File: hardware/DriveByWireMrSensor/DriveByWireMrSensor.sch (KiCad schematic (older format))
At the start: 7 parts, among them J1 Conn_01x04_Female, U1 LM358, U2 KMZ49_118

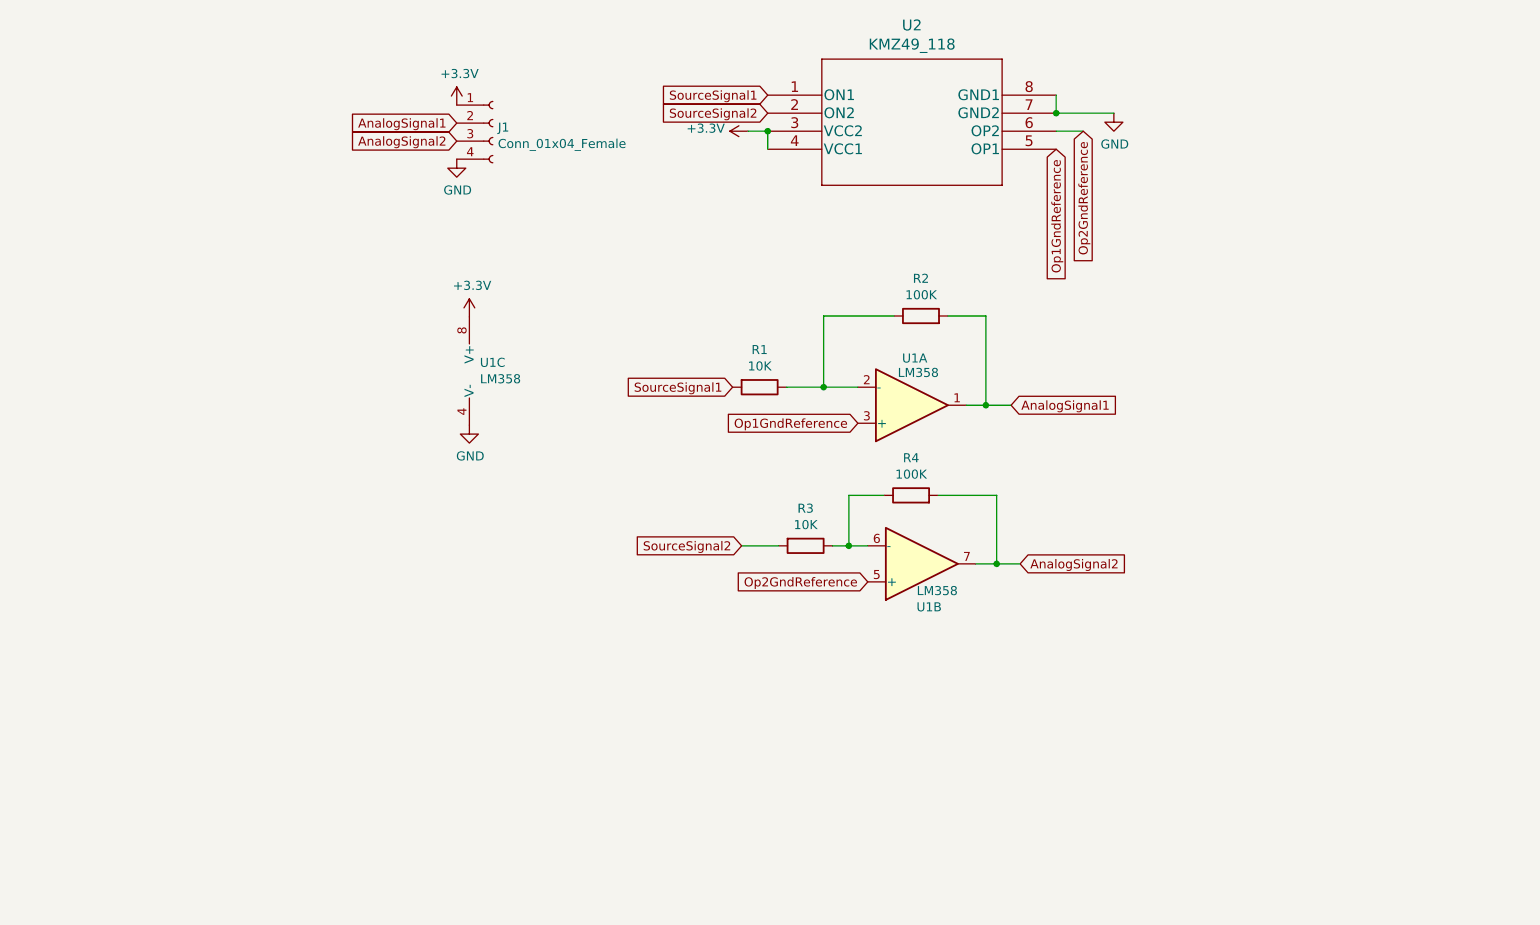
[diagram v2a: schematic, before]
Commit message: fixing drive by wire PCB to make space for shim and avoiding screw holes
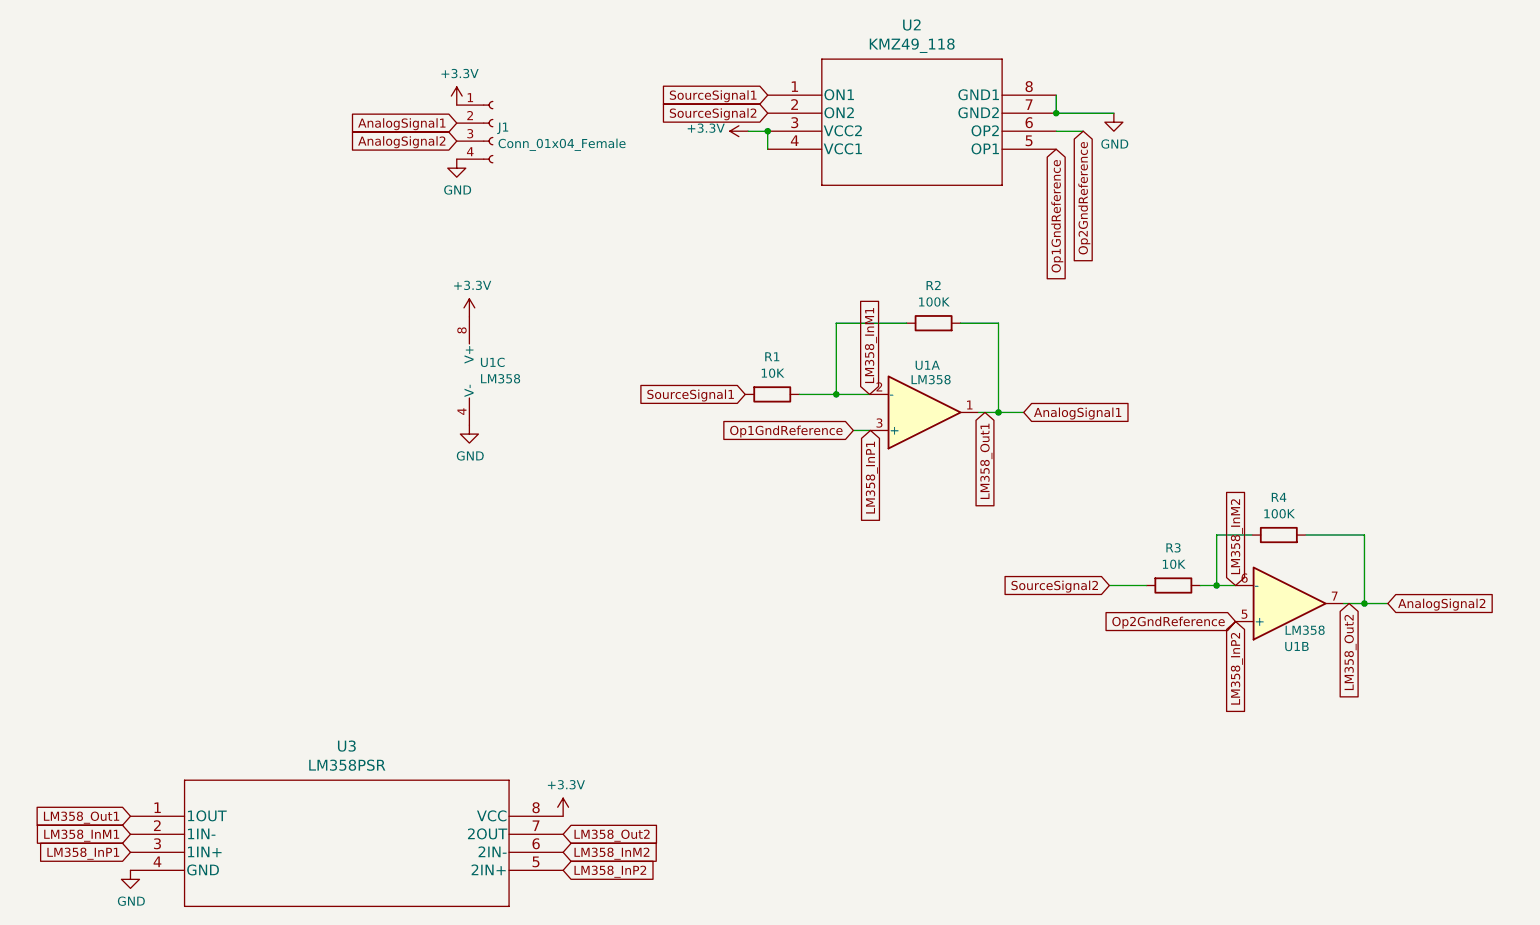
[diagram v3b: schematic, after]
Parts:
- added U3: LM358PSR, UsefulModifications:DFN-8-LM358, symbol LM358:LM358PSR
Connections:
- net +3V3: now also U3.8 (VCC)
- net AnalogSignal1: now also U3.1 (1OUT)
- net AnalogSignal2: now also U3.7 (2OUT)
- net GND: now also U3.4 (GND)
- net LM358_InM1: now reaches R1.1, R2.1, U1.2 (-)
- net LM358_InM1: now also U3.2 (1IN-)
- net LM358_InM2: now reaches R3.1, R4.1, U1.6 (-)
- net LM358_InM2: now also U3.6 (2IN-)
- net Op1GndReference renamed LM358_InP1
- net LM358_InP1: now also U3.3 (1IN+)
- net Op2GndReference renamed LM358_InP2
- net LM358_InP2: now also U3.5 (2IN+)
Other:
- moved on the sheet: R1, R2, R3, R4, U1A, U1B
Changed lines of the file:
@@
 L Device:R R1
 U 1 1 6189DE68
-P 5150 4080
-F 0 "R1" V 4943 4080 50  0000 C CNN
-F 1 "10K" V 5034 4080 50  0000 C CNN
-F 2 "Resistor_SMD:R_0805_2012Metric_Pad1.15x1.40mm_HandSolder" V 5080 4080 50  0001 C CNN
-F 3 "~" H 5150 4080 50  0001 C CNN
-	1    5150 4080
+P 5220 4120
+F 0 "R1" V 5013 4120 50  0000 C CNN
+F 1 "10K" V 5104 4120 50  0000 C CNN
+F 2 "Resistor_SMD:R_0805_2012Metric_Pad1.15x1.40mm_HandSolder" V 5150 4120 50  0001 C CNN
+F 3 "~" H 5220 4120 50  0001 C CNN
+	1    5220 4120
 	0    1    1    0
 $EndComp
@@
 L Device:R R2
 U 1 1 6189E497
-P 6045 3685
-F 0 "R2" V 6252 3685 50  0000 C CNN
-F 1 "100K" V 6161 3685 50  0000 C CNN
-F 2 "Resistor_SMD:R_0805_2012Metric_Pad1.15x1.40mm_HandSolder" V 5975 3685 50  0001 C CNN
-F 3 "~" H 6045 3685 50  0001 C CNN
-	1    6045 3685
+P 6115 3725
+F 0 "R2" V 6322 3725 50  0000 C CNN
+F 1 "100K" V 6231 3725 50  0000 C CNN
+F 2 "Resistor_SMD:R_0805_2012Metric_Pad1.15x1.40mm_HandSolder" V 6045 3725 50  0001 C CNN
+F 3 "~" H 6115 3725 50  0001 C CNN
+	1    6115 3725
 	0    -1   -1   0
 $EndComp
@@
 	1    0    0    -1
 $EndComp
-Text GLabel 6545 4180 2    50   Input ~ 0
+Text GLabel 6615 4220 2    50   Input ~ 0
 AnalogSignal1
 Text GLabel 6795 2760 3    50   Input ~ 0
 Op1GndReference
-Text GLabel 5695 4280 0    50   Input ~ 0
+Text GLabel 5670 4320 0    50   Input ~ 0
 Op1GndReference
 Text GLabel 5195 2460 0    50   Input ~ 0
 SourceSignal1
-Text GLabel 5000 4080 0    50   Input ~ 0
+Text GLabel 5070 4120 0    50   Input ~ 0
 SourceSignal1
 $Comp
 L Amplifier_Operational:LM358 U1
 U 1 1 618B4249
-P 5995 4180
-F 0 "U1" H 6010 3920 50  0000 C CNN
-F 1 "LM358" H 6030 4000 50  0000 C CNN
-F 2 "UsefulModifications:LM358PSR" H 5995 4180 50  0001 C CNN
-F 3 "http://www.ti.com/lit/ds/symlink/lm2904-n.pdf" H 5995 4180 50  0001 C CNN
-	1    5995 4180
+P 6065 4220
+F 0 "U1" H 6080 3960 50  0000 C CNN
+F 1 "LM358" H 6100 4040 50  0000 C CNN
+F 2 "UsefulModifications:LM358PSR" H 6065 4220 50  0001 C CNN
+F 3 "http://www.ti.com/lit/ds/symlink/lm2904-n.pdf" H 6065 4220 50  0001 C CNN
+	1    6065 4220
 	1    0    0    1
 $EndComp
@@
 $EndComp
 Wire Wire Line
-	6295 4180 6405 4180
-Wire Wire Line
-	6195 3685 6405 3685
-Wire Wire Line
-	6405 3685 6405 4180
-Connection ~ 6405 4180
-Wire Wire Line
-	6405 4180 6545 4180
-Wire Wire Line
-	5505 4080 5695 4080
-Wire Wire Line
-	5505 3685 5505 4080
-Wire Wire Line
-	5895 3685 5505 3685
-Wire Wire Line
-	5300 4080 5505 4080
-Connection ~ 5505 4080
+	6365 4220 6475 4220
+Wire Wire Line
+	6265 3725 6475 3725
+Wire Wire Line
+	6475 3725 6475 4220
+Connection ~ 6475 4220
+Wire Wire Line
+	6475 4220 6615 4220
+Wire Wire Line
+	5575 4120 5765 4120
+Wire Wire Line
+	5575 3725 5575 4120
+Wire Wire Line
+	5965 3725 5575 3725
+Wire Wire Line
+	5370 4120 5575 4120
+Connection ~ 5575 4120
 $Comp
 L power:+3.3V #PWR0106
@@
 L Amplifier_Operational:LM358 U1
 U 2 1 618E9970
-P 6050 5060
-F 0 "U1" H 6090 5300 50  0000 C CNN
-F 1 "LM358" H 6135 5210 50  0000 C CNN
-F 2 "UsefulModifications:LM358PSR" H 6050 5060 50  0001 C CNN
-F 3 "http://www.ti.com/lit/ds/symlink/lm2904-n.pdf" H 6050 5060 50  0001 C CNN
-	2    6050 5060
+P 8090 5280
+F 0 "U1" H 8130 5520 50  0000 C CNN
+F 1 "LM358" H 8175 5430 50  0000 C CNN
+F 2 "UsefulModifications:LM358PSR" H 8090 5280 50  0001 C CNN
+F 3 "http://www.ti.com/lit/ds/symlink/lm2904-n.pdf" H 8090 5280 50  0001 C CNN
+	2    8090 5280
 	1    0    0    1
 $EndComp
@@
 L Device:R R4
 U 1 1 618DED44
-P 5990 4680
-F 0 "R4" V 6197 4680 50  0000 C CNN
-F 1 "100K" V 6106 4680 50  0000 C CNN
-F 2 "Resistor_SMD:R_0805_2012Metric_Pad1.15x1.40mm_HandSolder" V 5920 4680 50  0001 C CNN
-F 3 "~" H 5990 4680 50  0001 C CNN
-	1    5990 4680
+P 8030 4900
+F 0 "R4" V 8237 4900 50  0000 C CNN
+F 1 "100K" V 8146 4900 50  0000 C CNN
+F 2 "Resistor_SMD:R_0805_2012Metric_Pad1.15x1.40mm_HandSolder" V 7960 4900 50  0001 C CNN
+F 3 "~" H 8030 4900 50  0001 C CNN
+	1    8030 4900
 	0    -1   -1   0
 $EndComp
@@
 L Device:R R3
 U 1 1 618E050D
-P 5405 4960
-F 0 "R3" V 5198 4960 50  0000 C CNN
-F 1 "10K" V 5289 4960 50  0000 C CNN
-F 2 "Resistor_SMD:R_0805_2012Metric_Pad1.15x1.40mm_HandSolder" V 5335 4960 50  0001 C CNN
-F 3 "~" H 5405 4960 50  0001 C CNN
-	1    5405 4960
+P 7445 5180
+F 0 "R3" V 7238 5180 50  0000 C CNN
+F 1 "10K" V 7329 5180 50  0000 C CNN
+F 2 "Resistor_SMD:R_0805_2012Metric_Pad1.15x1.40mm_HandSolder" V 7375 5180 50  0001 C CNN
+F 3 "~" H 7445 5180 50  0001 C CNN
+	1    7445 5180
 	0    1    1    0
 $EndComp
@@
 Text GLabel 5195 2560 0    50   Input ~ 0
 SourceSignal2
-Text GLabel 5050 4960 0    50   Input ~ 0
+Text GLabel 7090 5180 0    50   Input ~ 0
 SourceSignal2
-Text GLabel 5750 5160 0    50   Input ~ 0
+Text GLabel 7790 5380 0    50   Input ~ 0
 Op2GndReference
-Text GLabel 6595 5060 2    50   Input ~ 0
+Text GLabel 8635 5280 2    50   Input ~ 0
 AnalogSignal2
 Wire Wire Line
-	6350 5060 6465 5060
-Wire Wire Line
-	6140 4680 6465 4680
-Wire Wire Line
-	6465 4680 6465 5060
-Connection ~ 6465 5060
-Wire Wire Line
-	6465 5060 6595 5060
-Wire Wire Line
-	5555 4960 5645 4960
-Wire Wire Line
-	5840 4680 5645 4680
-Wire Wire Line
-	5645 4680 5645 4960
-Connection ~ 5645 4960
-Wire Wire Line
-	5645 4960 5750 4960
-Wire Wire Line
-	5050 4960 5255 4960
+	8390 5280 8505 5280
+Wire Wire Line
+	8180 4900 8505 4900
+Wire Wire Line
+	8505 4900 8505 5280
+Connection ~ 8505 5280
+Wire Wire Line
+	8505 5280 8635 5280
+Wire Wire Line
+	7595 5180 7685 5180
+Wire Wire Line
+	7880 4900 7685 4900
+Wire Wire Line
+	7685 4900 7685 5180
+Connection ~ 7685 5180
+Wire Wire Line
+	7685 5180 7790 5180
+Wire Wire Line
+	7090 5180 7295 5180
+$Comp
+L LM358:LM358PSR U3
+U 1 1 619970C4
+P 1660 6460
+F 0 "U3" H 2860 6847 60  0000 C CNN
+F 1 "LM358PSR" H 2860 6741 60  0000 C CNN
+F 2 "UsefulModifications:DFN-8-LM358" H 2860 6700 60  0001 C CNN
+F 3 "" H 1660 6460 60  0000 C CNN
+	1    1660 6460
+	1    0    0    -1
+$EndComp
+$Comp
+L power:GND #PWR0107
+U 1 1 61998A96
+P 1660 6760
+F 0 "#PWR0107" H 1660 6510 50  0001 C CNN
+F 1 "GND" H 1665 6587 50  0000 C CNN
+F 2 "" H 1660 6760 50  0001 C CNN
+F 3 "" H 1660 6760 50  0001 C CNN
+	1    1660 6760
+	1    0    0    -1
+$EndComp
+$Comp
+L power:+3.3V #PWR0108
+U 1 1 61999CB9
+P 4060 6460
+F 0 "#PWR0108" H 4060 6310 50  0001 C CNN
+F 1 "+3.3V" H 4075 6633 50  0000 C CNN
+F 2 "" H 4060 6460 50  0001 C CNN
+F 3 "" H 4060 6460 50  0001 C CNN
+	1    4060 6460
+	1    0    0    -1
+$EndComp
+Text GLabel 4060 6560 2    50   Input ~ 0
+LM358_Out2
+Text GLabel 4060 6660 2    50   Input ~ 0
+LM358_InM2
+Text GLabel 4060 6760 2    50   Input ~ 0
+LM358_InP2
+Text GLabel 1660 6460 0    50   Input ~ 0
+LM358_Out1
+Text GLabel 1660 6560 0    50   Input ~ 0
+LM358_InM1
+Text GLabel 1660 6660 0    50   Input ~ 0
+LM358_InP1
+Text GLabel 7790 5380 3    50   Input ~ 0
+LM358_InP2
+Text GLabel 8420 5280 3    50   Input ~ 0
+LM358_Out2
+Text GLabel 7790 5180 1    50   Input ~ 0
+LM358_InM2
+Text GLabel 6400 4220 3    50   Input ~ 0
+LM358_Out1
+Text GLabel 5760 4120 1    50   Input ~ 0
+LM358_InM1
+Text GLabel 5765 4320 3    50   Input ~ 0
+LM358_InP1
+Wire Wire Line
+	5765 4320 5670 4320
 $EndSCHEMATC
